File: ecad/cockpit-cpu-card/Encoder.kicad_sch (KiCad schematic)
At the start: 34 parts, among them J11 ENC1, J12 ENC2, U12 74HC165

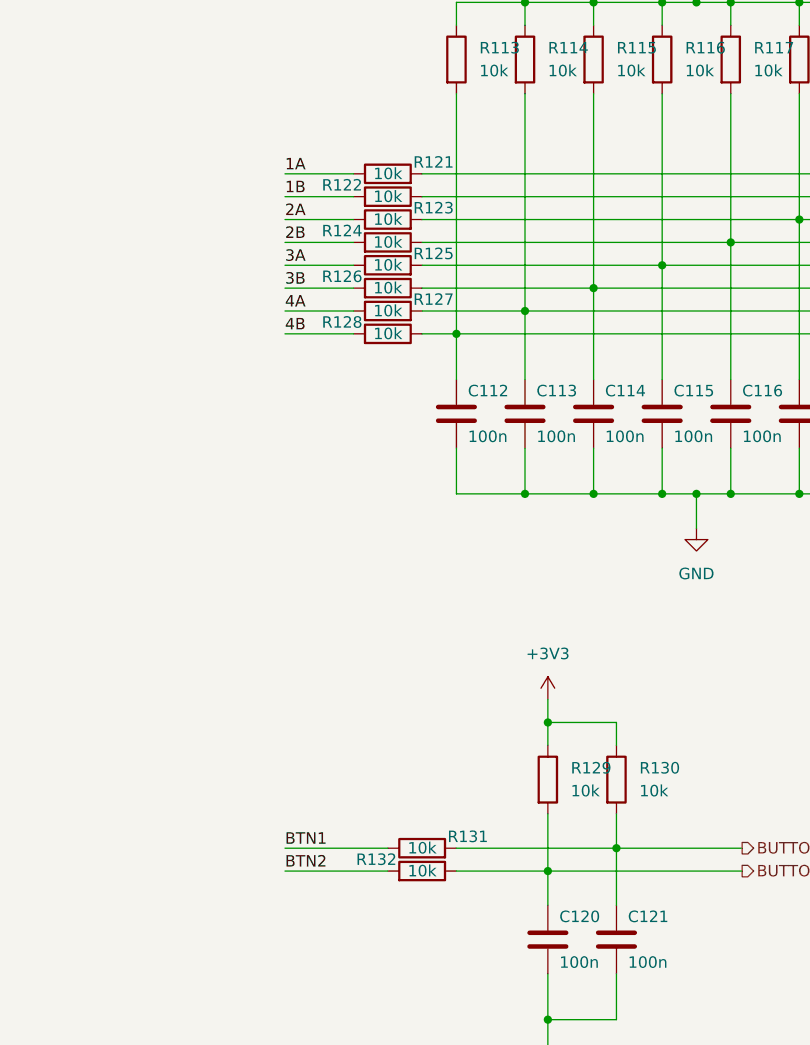
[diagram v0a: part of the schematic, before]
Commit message: Fixing wrong resistor values
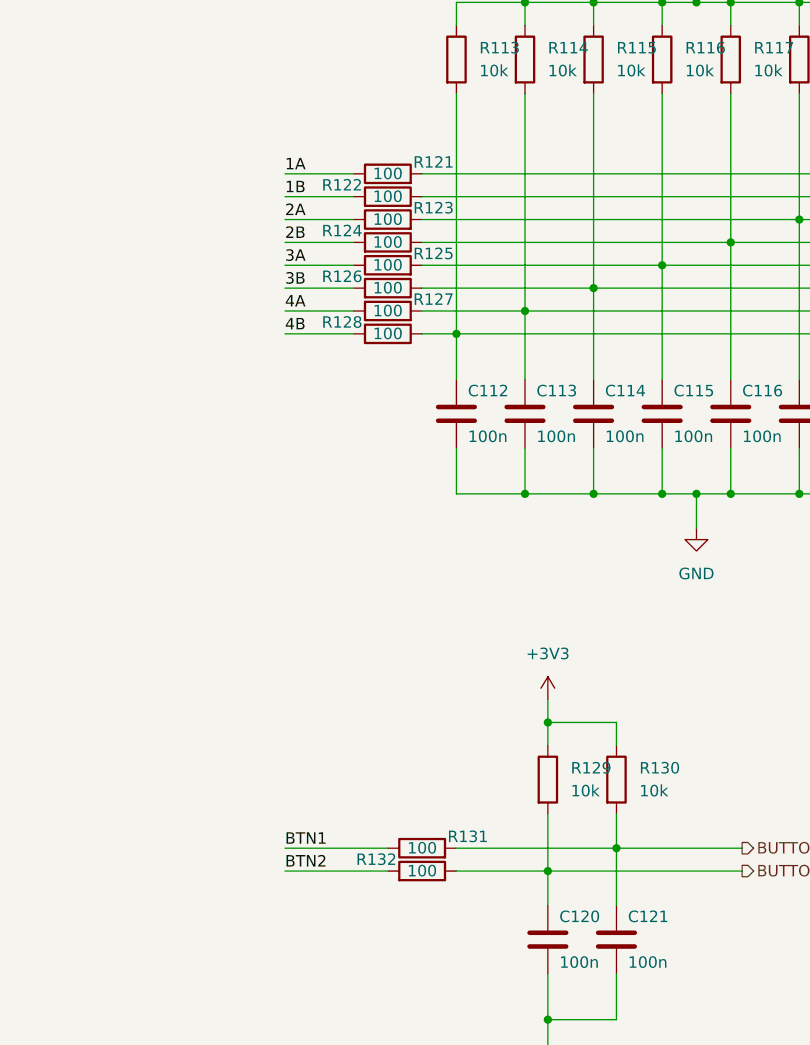
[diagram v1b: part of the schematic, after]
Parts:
- R121, R122, R123, R124, R125, R126, R127, R128, R131, R132: value 10k -> 100; MPN MCMR06X103 JTL -> MCMR06X1000FTL; ON_FARNELL 2073356 -> 2073347
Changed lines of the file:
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@@
     (in_bom yes) (on_board yes)
     (property "Reference" "R127" (id 0) (at 165.1 58.42 90))
-    (property "Value" "10k" (id 1) (at 160.02 59.69 90))
+    (property "Value" "100" (id 1) (at 160.02 59.69 90))
     (property "Footprint" "Resistor_SMD:R_0603_1608Metric" (id 2) (at 160.02 61.468 90)
       (effects (font (size 1.27 1.27)) hide)
@@
       (effects (font (size 1.27 1.27)) hide)
     )
-    (property "MPN" "MCMR06X103 JTL" (id 4) (at 160.02 59.69 0)
-      (effects (font (size 1.27 1.27)) hide)
-    )
-    (property "ON_FARNELL" "2073356" (id 5) (at 160.02 59.69 0)
+    (property "MPN" "MCMR06X1000FTL" (id 4) (at 160.02 59.69 0)
+      (effects (font (size 1.27 1.27)) hide)
+    )
+    (property "ON_FARNELL" "2073347" (id 5) (at 160.02 59.69 0)
       (effects (font (size 1.27 1.27)) hide)
     )
@@
     (in_bom yes) (on_board yes)
     (property "Reference" "R131" (id 0) (at 168.91 118.11 90))
-    (property "Value" "10k" (id 1) (at 163.83 119.38 90))
+    (property "Value" "100" (id 1) (at 163.83 119.38 90))
     (property "Footprint" "Resistor_SMD:R_0603_1608Metric" (id 2) (at 163.83 121.158 90)
       (effects (font (size 1.27 1.27)) hide)
@@
       (effects (font (size 1.27 1.27)) hide)
     )
-    (property "MPN" "MCMR06X103 JTL" (id 4) (at 163.83 119.38 0)
-      (effects (font (size 1.27 1.27)) hide)
-    )
-    (property "ON_FARNELL" "2073356" (id 5) (at 163.83 119.38 0)
+    (property "MPN" "MCMR06X1000FTL" (id 4) (at 163.83 119.38 0)
+      (effects (font (size 1.27 1.27)) hide)
+    )
+    (property "ON_FARNELL" "2073347" (id 5) (at 163.83 119.38 0)
       (effects (font (size 1.27 1.27)) hide)
     )
@@
     (in_bom yes) (on_board yes)
     (property "Reference" "R123" (id 0) (at 165.1 48.26 90))
-    (property "Value" "10k" (id 1) (at 160.02 49.53 90))
+    (property "Value" "100" (id 1) (at 160.02 49.53 90))
     (property "Footprint" "Resistor_SMD:R_0603_1608Metric" (id 2) (at 160.02 51.308 90)
       (effects (font (size 1.27 1.27)) hide)
@@
       (effects (font (size 1.27 1.27)) hide)
     )
-    (property "MPN" "MCMR06X103 JTL" (id 4) (at 160.02 49.53 0)
-      (effects (font (size 1.27 1.27)) hide)
-    )
-    (property "ON_FARNELL" "2073356" (id 5) (at 160.02 49.53 0)
+    (property "MPN" "MCMR06X1000FTL" (id 4) (at 160.02 49.53 0)
+      (effects (font (size 1.27 1.27)) hide)
+    )
+    (property "ON_FARNELL" "2073347" (id 5) (at 160.02 49.53 0)
       (effects (font (size 1.27 1.27)) hide)
     )
@@
     (in_bom yes) (on_board yes)
     (property "Reference" "R124" (id 0) (at 154.94 50.8 90))
-    (property "Value" "10k" (id 1) (at 160.02 52.07 90))
+    (property "Value" "100" (id 1) (at 160.02 52.07 90))
     (property "Footprint" "Resistor_SMD:R_0603_1608Metric" (id 2) (at 160.02 53.848 90)
       (effects (font (size 1.27 1.27)) hide)
@@
       (effects (font (size 1.27 1.27)) hide)
     )
-    (property "MPN" "MCMR06X103 JTL" (id 4) (at 160.02 52.07 0)
-      (effects (font (size 1.27 1.27)) hide)
-    )
-    (property "ON_FARNELL" "2073356" (id 5) (at 160.02 52.07 0)
+    (property "MPN" "MCMR06X1000FTL" (id 4) (at 160.02 52.07 0)
+      (effects (font (size 1.27 1.27)) hide)
+    )
+    (property "ON_FARNELL" "2073347" (id 5) (at 160.02 52.07 0)
       (effects (font (size 1.27 1.27)) hide)
     )
@@
     (in_bom yes) (on_board yes)
     (property "Reference" "R128" (id 0) (at 154.94 60.96 90))
-    (property "Value" "10k" (id 1) (at 160.02 62.23 90))
+    (property "Value" "100" (id 1) (at 160.02 62.23 90))
     (property "Footprint" "Resistor_SMD:R_0603_1608Metric" (id 2) (at 160.02 64.008 90)
       (effects (font (size 1.27 1.27)) hide)
@@
       (effects (font (size 1.27 1.27)) hide)
     )
-    (property "MPN" "MCMR06X103 JTL" (id 4) (at 160.02 62.23 0)
-      (effects (font (size 1.27 1.27)) hide)
-    )
-    (property "ON_FARNELL" "2073356" (id 5) (at 160.02 62.23 0)
+    (property "MPN" "MCMR06X1000FTL" (id 4) (at 160.02 62.23 0)
+      (effects (font (size 1.27 1.27)) hide)
+    )
+    (property "ON_FARNELL" "2073347" (id 5) (at 160.02 62.23 0)
       (effects (font (size 1.27 1.27)) hide)
     )
@@
     (in_bom yes) (on_board yes)
     (property "Reference" "R122" (id 0) (at 154.94 45.72 90))
-    (property "Value" "10k" (id 1) (at 160.02 46.99 90))
+    (property "Value" "100" (id 1) (at 160.02 46.99 90))
     (property "Footprint" "Resistor_SMD:R_0603_1608Metric" (id 2) (at 160.02 48.768 90)
       (effects (font (size 1.27 1.27)) hide)
@@
       (effects (font (size 1.27 1.27)) hide)
     )
-    (property "MPN" "MCMR06X103 JTL" (id 4) (at 160.02 46.99 0)
-      (effects (font (size 1.27 1.27)) hide)
-    )
-    (property "ON_FARNELL" "2073356" (id 5) (at 160.02 46.99 0)
+    (property "MPN" "MCMR06X1000FTL" (id 4) (at 160.02 46.99 0)
+      (effects (font (size 1.27 1.27)) hide)
+    )
+    (property "ON_FARNELL" "2073347" (id 5) (at 160.02 46.99 0)
       (effects (font (size 1.27 1.27)) hide)
     )
@@
     (in_bom yes) (on_board yes)
     (property "Reference" "R126" (id 0) (at 154.94 55.88 90))
-    (property "Value" "10k" (id 1) (at 160.02 57.15 90))
+    (property "Value" "100" (id 1) (at 160.02 57.15 90))
     (property "Footprint" "Resistor_SMD:R_0603_1608Metric" (id 2) (at 160.02 58.928 90)
       (effects (font (size 1.27 1.27)) hide)
@@
       (effects (font (size 1.27 1.27)) hide)
     )
-    (property "MPN" "MCMR06X103 JTL" (id 4) (at 160.02 57.15 0)
-      (effects (font (size 1.27 1.27)) hide)
-    )
-    (property "ON_FARNELL" "2073356" (id 5) (at 160.02 57.15 0)
+    (property "MPN" "MCMR06X1000FTL" (id 4) (at 160.02 57.15 0)
+      (effects (font (size 1.27 1.27)) hide)
+    )
+    (property "ON_FARNELL" "2073347" (id 5) (at 160.02 57.15 0)
       (effects (font (size 1.27 1.27)) hide)
     )
@@
     (in_bom yes) (on_board yes)
     (property "Reference" "R125" (id 0) (at 165.1 53.34 90))
-    (property "Value" "10k" (id 1) (at 160.02 54.61 90))
+    (property "Value" "100" (id 1) (at 160.02 54.61 90))
     (property "Footprint" "Resistor_SMD:R_0603_1608Metric" (id 2) (at 160.02 56.388 90)
       (effects (font (size 1.27 1.27)) hide)
@@
       (effects (font (size 1.27 1.27)) hide)
     )
-    (property "MPN" "MCMR06X103 JTL" (id 4) (at 160.02 54.61 0)
-      (effects (font (size 1.27 1.27)) hide)
-    )
-    (property "ON_FARNELL" "2073356" (id 5) (at 160.02 54.61 0)
+    (property "MPN" "MCMR06X1000FTL" (id 4) (at 160.02 54.61 0)
+      (effects (font (size 1.27 1.27)) hide)
+    )
+    (property "ON_FARNELL" "2073347" (id 5) (at 160.02 54.61 0)
       (effects (font (size 1.27 1.27)) hide)
     )
@@
     (in_bom yes) (on_board yes)
     (property "Reference" "R132" (id 0) (at 158.75 120.65 90))
-    (property "Value" "10k" (id 1) (at 163.83 121.92 90))
+    (property "Value" "100" (id 1) (at 163.83 121.92 90))
     (property "Footprint" "Resistor_SMD:R_0603_1608Metric" (id 2) (at 163.83 123.698 90)
       (effects (font (size 1.27 1.27)) hide)
@@
       (effects (font (size 1.27 1.27)) hide)
     )
-    (property "MPN" "MCMR06X103 JTL" (id 4) (at 163.83 121.92 0)
-      (effects (font (size 1.27 1.27)) hide)
-    )
-    (property "ON_FARNELL" "2073356" (id 5) (at 163.83 121.92 0)
+    (property "MPN" "MCMR06X1000FTL" (id 4) (at 163.83 121.92 0)
+      (effects (font (size 1.27 1.27)) hide)
+    )
+    (property "ON_FARNELL" "2073347" (id 5) (at 163.83 121.92 0)
       (effects (font (size 1.27 1.27)) hide)
     )
@@
     (in_bom yes) (on_board yes)
     (property "Reference" "R121" (id 0) (at 165.1 43.18 90))
-    (property "Value" "10k" (id 1) (at 160.02 44.45 90))
+    (property "Value" "100" (id 1) (at 160.02 44.45 90))
     (property "Footprint" "Resistor_SMD:R_0603_1608Metric" (id 2) (at 160.02 46.228 90)
       (effects (font (size 1.27 1.27)) hide)
@@
       (effects (font (size 1.27 1.27)) hide)
     )
-    (property "MPN" "MCMR06X103 JTL" (id 4) (at 160.02 44.45 0)
-      (effects (font (size 1.27 1.27)) hide)
-    )
-    (property "ON_FARNELL" "2073356" (id 5) (at 160.02 44.45 0)
-      (effects (font (size 1.27 1.27)) hide)
-    )
+    (property "MPN" "MCMR06X1000FTL" (id 4) (at 160.02 44.45 0)
+      (effects (font (size 1.27 1.27)) hide)
+    )
+    (property "ON_FARNELL" "2073347" (id 5) (at 160.02 44.45 0)
+      (effects (font (size 1.27 1.27)) hide)
+    )

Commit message: 120R from Distrelec
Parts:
- R121, R122, R123, R124, R125, R126, R127, R128, R131, R132: value 100 -> 120; MPN MCMR06X1000FTL -> 1550603SAF1200T5E; ON_DISTRELEC (none) -> 300-56-474; ON_FARNELL 2073347 -> (none)
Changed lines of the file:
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@@
     (in_bom yes) (on_board yes)
     (property "Reference" "R127" (id 0) (at 165.1 58.42 90))
-    (property "Value" "100" (id 1) (at 160.02 59.69 90))
+    (property "Value" "120" (id 1) (at 160.02 59.69 90))
     (property "Footprint" "Resistor_SMD:R_0603_1608Metric" (id 2) (at 160.02 61.468 90)
       (effects (font (size 1.27 1.27)) hide)
@@
       (effects (font (size 1.27 1.27)) hide)
     )
-    (property "MPN" "MCMR06X1000FTL" (id 4) (at 160.02 59.69 0)
-      (effects (font (size 1.27 1.27)) hide)
-    )
-    (property "ON_FARNELL" "2073347" (id 5) (at 160.02 59.69 0)
+    (property "MPN" "1550603SAF1200T5E" (id 4) (at 160.02 59.69 0)
+      (effects (font (size 1.27 1.27)) hide)
+    )
+    (property "ON_FARNELL" "" (id 5) (at 160.02 59.69 0)
+      (effects (font (size 1.27 1.27)) hide)
+    )
+    (property "ON_DISTRELEC" "300-56-474" (id 6) (at 160.02 59.69 0)
       (effects (font (size 1.27 1.27)) hide)
     )
@@
     (in_bom yes) (on_board yes)
     (property "Reference" "R131" (id 0) (at 168.91 118.11 90))
-    (property "Value" "100" (id 1) (at 163.83 119.38 90))
+    (property "Value" "120" (id 1) (at 163.83 119.38 90))
     (property "Footprint" "Resistor_SMD:R_0603_1608Metric" (id 2) (at 163.83 121.158 90)
       (effects (font (size 1.27 1.27)) hide)
@@
       (effects (font (size 1.27 1.27)) hide)
     )
-    (property "MPN" "MCMR06X1000FTL" (id 4) (at 163.83 119.38 0)
-      (effects (font (size 1.27 1.27)) hide)
-    )
-    (property "ON_FARNELL" "2073347" (id 5) (at 163.83 119.38 0)
+    (property "MPN" "1550603SAF1200T5E" (id 4) (at 163.83 119.38 0)
+      (effects (font (size 1.27 1.27)) hide)
+    )
+    (property "ON_FARNELL" "" (id 5) (at 163.83 119.38 0)
+      (effects (font (size 1.27 1.27)) hide)
+    )
+    (property "ON_DISTRELEC" "300-56-474" (id 6) (at 163.83 119.38 0)
       (effects (font (size 1.27 1.27)) hide)
     )
@@
     (in_bom yes) (on_board yes)
     (property "Reference" "R123" (id 0) (at 165.1 48.26 90))
-    (property "Value" "100" (id 1) (at 160.02 49.53 90))
+    (property "Value" "120" (id 1) (at 160.02 49.53 90))
     (property "Footprint" "Resistor_SMD:R_0603_1608Metric" (id 2) (at 160.02 51.308 90)
       (effects (font (size 1.27 1.27)) hide)
@@
       (effects (font (size 1.27 1.27)) hide)
     )
-    (property "MPN" "MCMR06X1000FTL" (id 4) (at 160.02 49.53 0)
-      (effects (font (size 1.27 1.27)) hide)
-    )
-    (property "ON_FARNELL" "2073347" (id 5) (at 160.02 49.53 0)
+    (property "MPN" "1550603SAF1200T5E" (id 4) (at 160.02 49.53 0)
+      (effects (font (size 1.27 1.27)) hide)
+    )
+    (property "ON_FARNELL" "" (id 5) (at 160.02 49.53 0)
+      (effects (font (size 1.27 1.27)) hide)
+    )
+    (property "ON_DISTRELEC" "300-56-474" (id 6) (at 160.02 49.53 0)
       (effects (font (size 1.27 1.27)) hide)
     )
@@
     (in_bom yes) (on_board yes)
     (property "Reference" "R124" (id 0) (at 154.94 50.8 90))
-    (property "Value" "100" (id 1) (at 160.02 52.07 90))
+    (property "Value" "120" (id 1) (at 160.02 52.07 90))
     (property "Footprint" "Resistor_SMD:R_0603_1608Metric" (id 2) (at 160.02 53.848 90)
       (effects (font (size 1.27 1.27)) hide)
@@
       (effects (font (size 1.27 1.27)) hide)
     )
-    (property "MPN" "MCMR06X1000FTL" (id 4) (at 160.02 52.07 0)
-      (effects (font (size 1.27 1.27)) hide)
-    )
-    (property "ON_FARNELL" "2073347" (id 5) (at 160.02 52.07 0)
+    (property "MPN" "1550603SAF1200T5E" (id 4) (at 160.02 52.07 0)
+      (effects (font (size 1.27 1.27)) hide)
+    )
+    (property "ON_FARNELL" "" (id 5) (at 160.02 52.07 0)
+      (effects (font (size 1.27 1.27)) hide)
+    )
+    (property "ON_DISTRELEC" "300-56-474" (id 6) (at 160.02 52.07 0)
       (effects (font (size 1.27 1.27)) hide)
     )
@@
     (in_bom yes) (on_board yes)
     (property "Reference" "R128" (id 0) (at 154.94 60.96 90))
-    (property "Value" "100" (id 1) (at 160.02 62.23 90))
+    (property "Value" "120" (id 1) (at 160.02 62.23 90))
     (property "Footprint" "Resistor_SMD:R_0603_1608Metric" (id 2) (at 160.02 64.008 90)
       (effects (font (size 1.27 1.27)) hide)
@@
       (effects (font (size 1.27 1.27)) hide)
     )
-    (property "MPN" "MCMR06X1000FTL" (id 4) (at 160.02 62.23 0)
-      (effects (font (size 1.27 1.27)) hide)
-    )
-    (property "ON_FARNELL" "2073347" (id 5) (at 160.02 62.23 0)
+    (property "MPN" "1550603SAF1200T5E" (id 4) (at 160.02 62.23 0)
+      (effects (font (size 1.27 1.27)) hide)
+    )
+    (property "ON_FARNELL" "" (id 5) (at 160.02 62.23 0)
+      (effects (font (size 1.27 1.27)) hide)
+    )
+    (property "ON_DISTRELEC" "300-56-474" (id 6) (at 160.02 62.23 0)
       (effects (font (size 1.27 1.27)) hide)
     )
@@
     (in_bom yes) (on_board yes)
     (property "Reference" "R122" (id 0) (at 154.94 45.72 90))
-    (property "Value" "100" (id 1) (at 160.02 46.99 90))
+    (property "Value" "120" (id 1) (at 160.02 46.99 90))
     (property "Footprint" "Resistor_SMD:R_0603_1608Metric" (id 2) (at 160.02 48.768 90)
       (effects (font (size 1.27 1.27)) hide)
@@
       (effects (font (size 1.27 1.27)) hide)
     )
-    (property "MPN" "MCMR06X1000FTL" (id 4) (at 160.02 46.99 0)
-      (effects (font (size 1.27 1.27)) hide)
-    )
-    (property "ON_FARNELL" "2073347" (id 5) (at 160.02 46.99 0)
+    (property "MPN" "1550603SAF1200T5E" (id 4) (at 160.02 46.99 0)
+      (effects (font (size 1.27 1.27)) hide)
+    )
+    (property "ON_FARNELL" "" (id 5) (at 160.02 46.99 0)
+      (effects (font (size 1.27 1.27)) hide)
+    )
+    (property "ON_DISTRELEC" "300-56-474" (id 6) (at 160.02 46.99 0)
       (effects (font (size 1.27 1.27)) hide)
     )
@@
     (in_bom yes) (on_board yes)
     (property "Reference" "R126" (id 0) (at 154.94 55.88 90))
-    (property "Value" "100" (id 1) (at 160.02 57.15 90))
+    (property "Value" "120" (id 1) (at 160.02 57.15 90))
     (property "Footprint" "Resistor_SMD:R_0603_1608Metric" (id 2) (at 160.02 58.928 90)
       (effects (font (size 1.27 1.27)) hide)
@@
       (effects (font (size 1.27 1.27)) hide)
     )
-    (property "MPN" "MCMR06X1000FTL" (id 4) (at 160.02 57.15 0)
-      (effects (font (size 1.27 1.27)) hide)
-    )
-    (property "ON_FARNELL" "2073347" (id 5) (at 160.02 57.15 0)
+    (property "MPN" "1550603SAF1200T5E" (id 4) (at 160.02 57.15 0)
+      (effects (font (size 1.27 1.27)) hide)
+    )
+    (property "ON_FARNELL" "" (id 5) (at 160.02 57.15 0)
+      (effects (font (size 1.27 1.27)) hide)
+    )
+    (property "ON_DISTRELEC" "300-56-474" (id 6) (at 160.02 57.15 0)
       (effects (font (size 1.27 1.27)) hide)
     )
@@
     (in_bom yes) (on_board yes)
     (property "Reference" "R125" (id 0) (at 165.1 53.34 90))
-    (property "Value" "100" (id 1) (at 160.02 54.61 90))
+    (property "Value" "120" (id 1) (at 160.02 54.61 90))
     (property "Footprint" "Resistor_SMD:R_0603_1608Metric" (id 2) (at 160.02 56.388 90)
       (effects (font (size 1.27 1.27)) hide)
@@
       (effects (font (size 1.27 1.27)) hide)
     )
-    (property "MPN" "MCMR06X1000FTL" (id 4) (at 160.02 54.61 0)
-      (effects (font (size 1.27 1.27)) hide)
-    )
-    (property "ON_FARNELL" "2073347" (id 5) (at 160.02 54.61 0)
+    (property "MPN" "1550603SAF1200T5E" (id 4) (at 160.02 54.61 0)
+      (effects (font (size 1.27 1.27)) hide)
+    )
+    (property "ON_FARNELL" "" (id 5) (at 160.02 54.61 0)
+      (effects (font (size 1.27 1.27)) hide)
+    )
+    (property "ON_DISTRELEC" "300-56-474" (id 6) (at 160.02 54.61 0)
       (effects (font (size 1.27 1.27)) hide)
     )
@@
     (in_bom yes) (on_board yes)
     (property "Reference" "R132" (id 0) (at 158.75 120.65 90))
-    (property "Value" "100" (id 1) (at 163.83 121.92 90))
+    (property "Value" "120" (id 1) (at 163.83 121.92 90))
     (property "Footprint" "Resistor_SMD:R_0603_1608Metric" (id 2) (at 163.83 123.698 90)
       (effects (font (size 1.27 1.27)) hide)
@@
       (effects (font (size 1.27 1.27)) hide)
     )
-    (property "MPN" "MCMR06X1000FTL" (id 4) (at 163.83 121.92 0)
-      (effects (font (size 1.27 1.27)) hide)
-    )
-    (property "ON_FARNELL" "2073347" (id 5) (at 163.83 121.92 0)
+    (property "MPN" "1550603SAF1200T5E" (id 4) (at 163.83 121.92 0)
+      (effects (font (size 1.27 1.27)) hide)
+    )
+    (property "ON_FARNELL" "" (id 5) (at 163.83 121.92 0)
+      (effects (font (size 1.27 1.27)) hide)
+    )
+    (property "ON_DISTRELEC" "300-56-474" (id 6) (at 163.83 121.92 0)
       (effects (font (size 1.27 1.27)) hide)
     )
@@
     (in_bom yes) (on_board yes)
     (property "Reference" "R121" (id 0) (at 165.1 43.18 90))
-    (property "Value" "100" (id 1) (at 160.02 44.45 90))
+    (property "Value" "120" (id 1) (at 160.02 44.45 90))
     (property "Footprint" "Resistor_SMD:R_0603_1608Metric" (id 2) (at 160.02 46.228 90)
       (effects (font (size 1.27 1.27)) hide)
@@
       (effects (font (size 1.27 1.27)) hide)
     )
-    (property "MPN" "MCMR06X1000FTL" (id 4) (at 160.02 44.45 0)
-      (effects (font (size 1.27 1.27)) hide)
-    )
-    (property "ON_FARNELL" "2073347" (id 5) (at 160.02 44.45 0)
-      (effects (font (size 1.27 1.27)) hide)
-    )
+    (property "MPN" "1550603SAF1200T5E" (id 4) (at 160.02 44.45 0)
+      (effects (font (size 1.27 1.27)) hide)
+    )
+    (property "ON_FARNELL" "" (id 5) (at 160.02 44.45 0)
+      (effects (font (size 1.27 1.27)) hide)
+    )
+    (property "ON_DISTRELEC" "300-56-474" (id 6) (at 160.02 44.45 0)
+      (effects (font (size 1.27 1.27)) hide)
+    )
